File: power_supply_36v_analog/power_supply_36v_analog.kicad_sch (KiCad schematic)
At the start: 0 parts

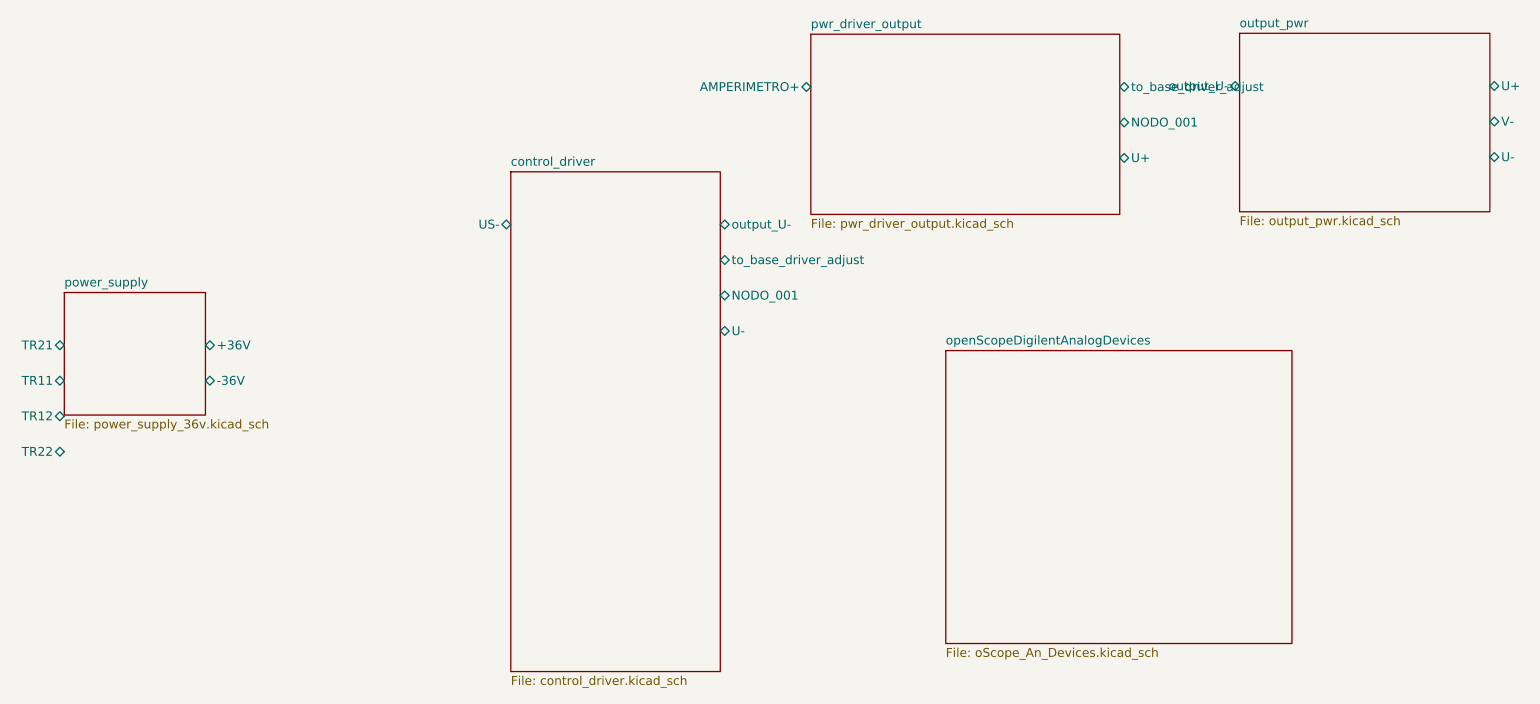
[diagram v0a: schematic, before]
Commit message: Fix pin spacing to 2.54mm like DiscoveryAnalog3 sheet
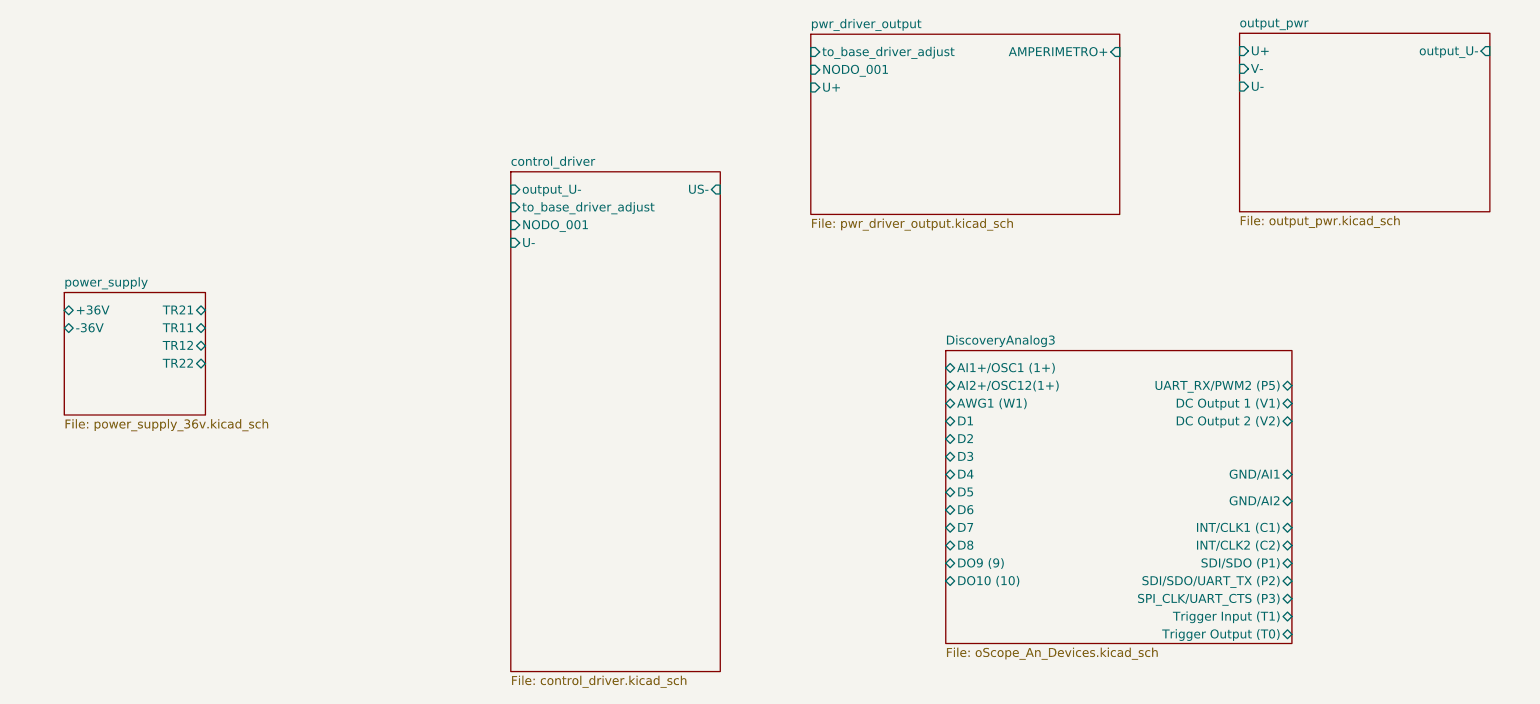
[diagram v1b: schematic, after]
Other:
- sheet openScopeDigilentAnalogDevices renamed DiscoveryAnalog3
- sheet DiscoveryAnalog3 ports: added AI1+/OSC1 (1+), AI2+/OSC12(1+), AWG1 (W1), D1, D2, D3, D4, D5, D6, D7, D8, DC Output 1 (V1), DC Output 2 (V2), DO10 (10), DO9 (9), GND/AI1, GND/AI2, INT/CLK1 (C1), INT/CLK2 (C2), SDI/SDO (P1), SDI/SDO/UART_TX (P2), SPI_CLK/UART_CTS (P3), Trigger Input (T1), Trigger Output (T0), UART_RX/PWM2 (P5); removed none
